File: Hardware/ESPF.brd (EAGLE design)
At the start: 30 x 20 mm, 24 parts, among them IC1 CP2102N-A01-GQFN24, J2 USB-C-16P-16P, J3 ESP-PROG-1X6-2.54-PINS-RA, Q1 MMDT3904

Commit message: Replace ESPFlash header using part from dedicated library.
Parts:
- FID1, FID2: device freetronics:FIDUCIAL-1X2.5 -> SuperHouse-Symbols:FIDUCIAL-1X2.5
- J3: value ESP-PROG-1X6-2.54-PINS-RA -> ESPFLASH-1X6-2.54-PINS-RA; device SuperHouse-ESP-Prog:1X6-2.54-PINS-RA -> SuperHouse-ESPFlash:1X6-2.54-PINS-RA
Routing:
- net GND: track 7.24 -> 6.39 mm
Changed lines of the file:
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@@
 <?xml version="1.0" encoding="utf-8"?>
 <!DOCTYPE eagle SYSTEM "eagle.dtd">
-<eagle version="9.6.1">
+<eagle version="9.6.2">
 <drawing>
 <settings>
-<setting alwaysvectorfont="no"/>
+<setting alwaysvectorfont="yes"/>
 <setting keepoldvectorfont="yes"/>
 <setting verticaltext="up"/>
@@
 </layers>
 <board>
-<fusionsync huburn="a.cGVyc29uYWw6dWUyZDliZmNi" projecturn="a.cGVyc29uYWw6dWUyZDliZmNiIzIwMTkwNjE5MTk5NjgzNjgx" f3durn="urn:adsk.wipprod:dm.lineage:swBH170zRHaojB2h5Vblyg" pcbguid="65d1a610-0e94-4f7e-955b-cbe41dc31425" lastpulledtime="" lastsyncedchangeguid="8f27d1c3-c2be-d358-18db-d89d43a70d9e" latestrevisionid="fcdf8aa0-1bba-404e-aedf-1c9e20859707" lastsyncedrevisionid="fcdf8aa0-1bba-404e-aedf-1c9e20859707" lastboardhashguid="c79eb5d4-1c34-d8a5-41d2-598309a68487" lastpushedtime="2020-05-26T02:52:23Z" linktopcb3d="%12"/>
+<fusionsync huburn="a.cGVyc29uYWw6dWUyZDliZmNi" projecturn="a.cGVyc29uYWw6dWUyZDliZmNiIzIwMTkwNjE5MTk5NjgzNjgx" f3durn="urn:adsk.wipprod:dm.lineage:swBH170zRHaojB2h5Vblyg" pcbguid="" lastpulledtime="" lastsyncedchangeguid="8f27d1c3-c2be-d358-18db-d89d43a70d9e" latestrevisionid="91da5424-9410-462b-9c00-ecb5205e71c2" lastsyncedrevisionid="91da5424-9410-462b-9c00-ecb5205e71c2" lastboardhashguid="118d0222-e689-2150-c329-ce3e1fc67ca0" lastpushedtime="2021-03-05T03:46:09Z" linktopcb3d="true"/>
 <plain>
 <text x="10.25" y="18.55" size="1.2" layer="21" font="vector" ratio="18">superhouse.tv/espf</text>
@@
 <attribute name="VALUE" x="10.0348" y="12.516" size="0.4064" layer="27" font="vector" rot="R270"/>
 </element>
-<element name="FID1" library="freetronics" package="FIDUCIAL-1X2.5" value="FIDUCIAL1X2.5" x="2.5" y="8.5" smashed="yes"/>
-<element name="FID2" library="freetronics" package="FIDUCIAL-1X2.5" value="FIDUCIAL1X2.5" x="21" y="16.5" smashed="yes"/>
-<element name="J3" library="SuperHouse-ESP-Prog" library_urn="urn:adsk.eagle:library:14353672" package="1X6-2.54-PINS-RA" package3d_urn="urn:adsk.eagle:package:20465662/6" value="ESP-PROG-1X6-2.54-PINS-RA" x="20.7" y="1.6" smashed="yes">
+<element name="FID1" library="SuperHouse-Symbols" library_urn="urn:adsk.eagle:library:13228893" package="FIDUCIAL-1X2.5" package3d_urn="urn:adsk.eagle:package:13228898/2" value="FIDUCIAL1X2.5" x="2.5" y="8.5" smashed="yes"/>
+<element name="FID2" library="SuperHouse-Symbols" library_urn="urn:adsk.eagle:library:13228893" package="FIDUCIAL-1X2.5" package3d_urn="urn:adsk.eagle:package:13228898/2" value="FIDUCIAL1X2.5" x="21" y="16.5" smashed="yes"/>
+<element name="J3" library="SuperHouse-ESPFlash" library_urn="urn:adsk.eagle:library:23117902" package="1X6-2.54-PINS-RA" package3d_urn="urn:adsk.eagle:package:20465662/7" value="ESPFLASH-1X6-2.54-PINS-RA" x="20.7" y="1.6" smashed="yes">
 <attribute name="NAME" x="20.7" y="3.4288" size="1.27" layer="25" font="vector" ratio="10" align="bottom-center"/>
 </element>
@@
 <contactref element="C3" pad="2"/>
 <contactref element="C2" pad="2"/>
-<wire x1="15.1" y1="9.75" x2="17.25" y2="9.75" width="0.254" layer="1"/>
-<wire x1="17.25" y1="9.75" x2="17.5" y2="9.5" width="0.254" layer="1"/>
+<wire x1="15.1" y1="9.75" x2="16.75" y2="9.75" width="0.254" layer="1"/>
 <wire x1="15.1" y1="9.75" x2="14.25" y2="9.75" width="0.254" layer="1"/>
 <wire x1="14.25" y1="9.75" x2="14" y2="10" width="0.254" layer="1"/>
@@
 <wire x1="6.68" y1="5.68" x2="6.18" y2="5.68" width="0.508" layer="1"/>
 <wire x1="7.095" y1="6.095" x2="6.68" y2="5.68" width="0.508" layer="1"/>
-<wire x1="17.5" y1="9.5" x2="17" y2="9" width="0" layer="19" extent="1-1"/>
+<wire x1="16.75" y1="9.75" x2="17" y2="9" width="0" layer="19" extent="1-1"/>
 </signal>
 <signal name="D-">

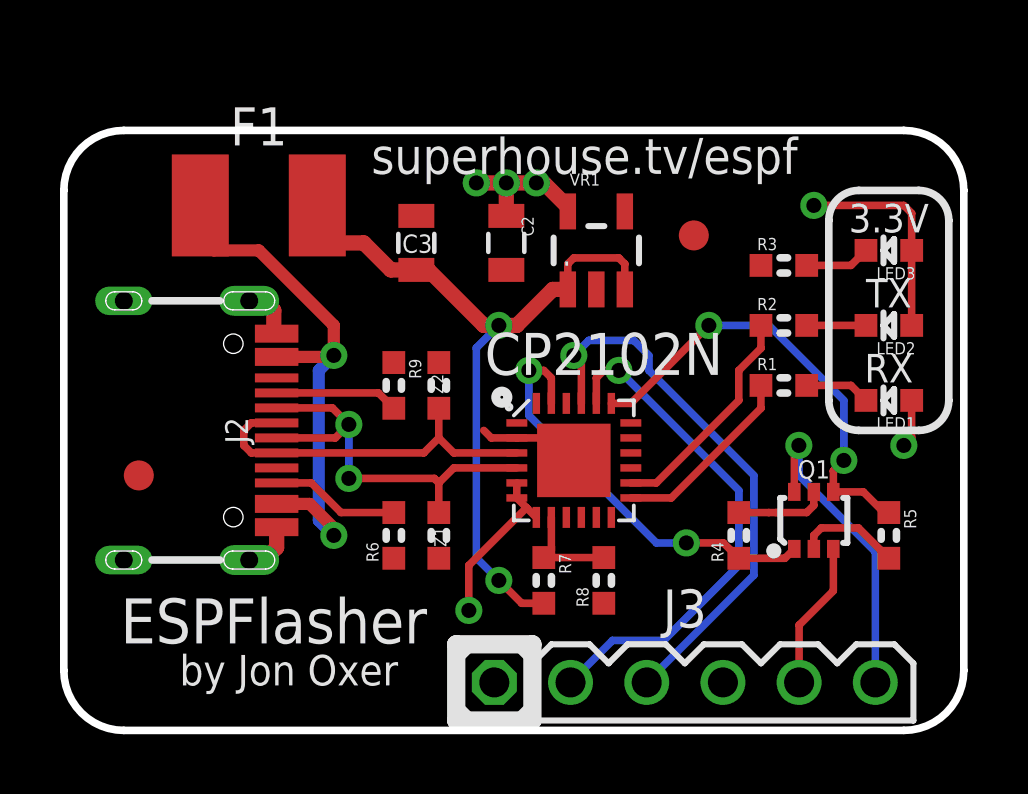
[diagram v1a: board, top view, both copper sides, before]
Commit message: Added 100nF cap on reset line of target device. Added tab to support right angle header. Added note about ESPFlash convention in schematic.
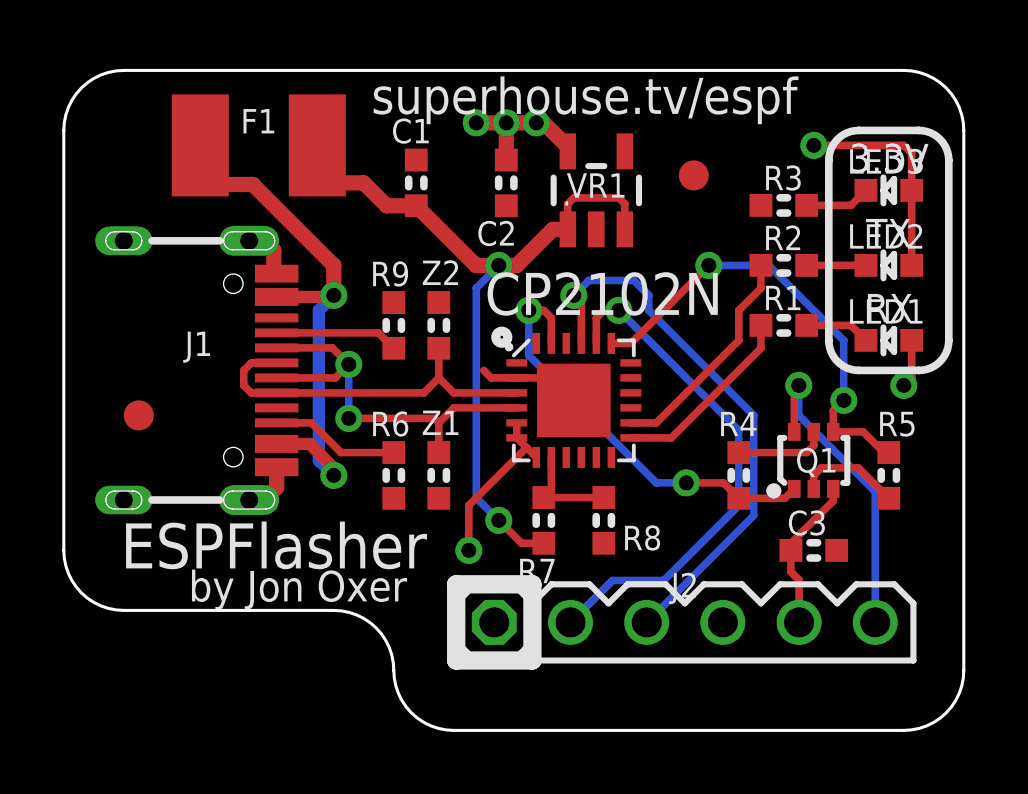
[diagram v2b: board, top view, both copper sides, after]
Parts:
- removed J3: ESPFLASH-1X6-2.54-PINS-RA, SuperHouse-ESPFlash:1X6-2.54-PINS-RA
- added C1: 10uF, SuperHouse-DiscreteSemi:C0603
- added J1: USB-C-16P-16P, SuperHouse-Connectors:USB-C-16P
- C2: device SuperHouse-DiscreteSemi:C0805 -> SuperHouse-DiscreteSemi:C0603
- C3: value 10uF -> 100nF; device SuperHouse-DiscreteSemi:C0805 -> SuperHouse-DiscreteSemi:C0603
- J2: value USB-C-16P-16P -> ESPFLASH-1X6-2.54-PINS-RA; device SuperHouse-Connectors:USB-C-16P -> SuperHouse-ESPFlash:1X6-2.54-PINS-RA
- VR1: value AP2112KSOT25 -> AP2112K-3.3
- moved J2 19.8 mm to (20.7, 3.60), turned to 0 degrees
- moved C3 16.8 mm to (25.0, 6.00), turned to 0 degrees
- moved C2 2.00 mm to (14.8, 18.2)
- moved F1 2.00 mm to (6.50, 19.5)
- moved FID1 2.00 mm to (2.50, 10.5)
- moved FID2 2.00 mm to (21.0, 18.5)
- moved IC1 2.00 mm to (17.0, 11.0)
- moved LED1 2.00 mm to (27.5, 13.0)
- moved LED2 2.00 mm to (27.5, 15.5)
- moved LED3 2.00 mm to (27.5, 18.0)
- moved Q1 2.00 mm to (25.0, 9.00)
- moved R1 2.00 mm to (24.0, 13.5)
- moved R2 2.00 mm to (24.0, 15.5)
- moved R3 2.00 mm to (24.0, 17.5)
- moved R4 2.00 mm to (22.5, 8.50)
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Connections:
- net 3.3V: now also J2.4; no longer J3.4
- net 5V: now also C1.1; no longer C3.1
- net D+: now also J1.A6, J1.B6; no longer J2.A6, J2.B6
- net D-: now also J1.A7, J1.B7; no longer J2.A7, J2.B7
- net EN: now also C3.1, J2.5; no longer J3.5
- net GND: now also C1.2, J1.A12B1, J1.A1B12, J1.FIX1, J1.FIX2, J1.FIX3, J1.FIX4, J2.1; no longer J2.A12B1, J2.A1B12, J2.FIX1, J2.FIX2, J2.FIX3, J2.FIX4, J3.1
- net GPIO0: now also J2.6; no longer J3.6
- net N$10: now also J1.A5; no longer J2.A5
- net N$9: now also J1.B5; no longer J2.B5
- net RXI: now also J2.2; no longer J3.2
- net TXO: now also J2.3; no longer J3.3
- net VIN: now also J1.A4B9, J1.A9B4; no longer J2.A4B9, J2.A9B4
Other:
- board size 30 x 20 mm -> 30 x 22 mm
- board text added: "(C) 2019-2021 SuperHouse Automation Released under the TAPR Open Hardware License www.tapr.org/OHL"
- board text added: "v3.2"
- board text removed: "Copyright 2020 SuperHouse Automation Released under the TAPR Open Hardware License www.tapr.org/OHL"
- board text removed: "v3.0"
